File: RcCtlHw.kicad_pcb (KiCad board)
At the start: 2 copper layers, 26.7 x 41.9 mm, 30 parts, among them J1 USB_B_Mini, J2 Program, J3 TFT_LCD, SW1 On/Off, U1 TP4056, U2 ESP-M2, U3 ADS1015, U4 Joystick

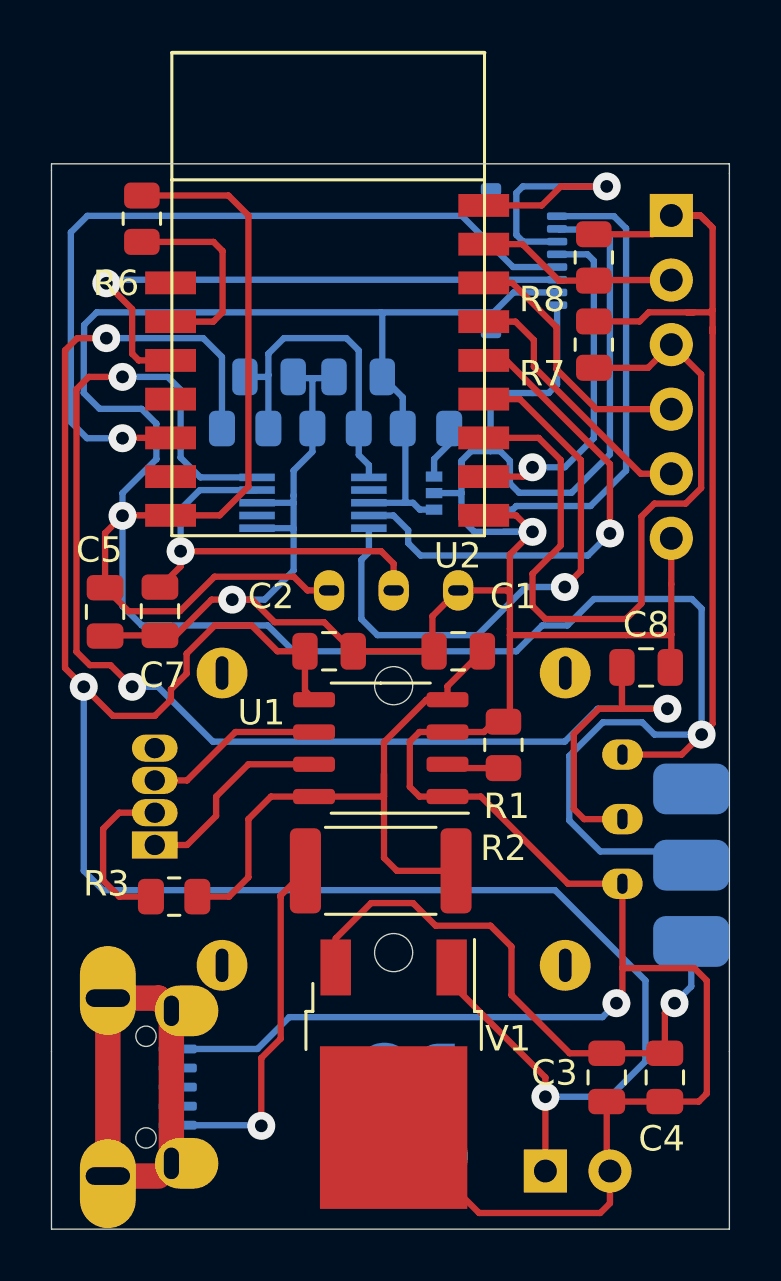
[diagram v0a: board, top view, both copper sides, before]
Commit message: Space things out
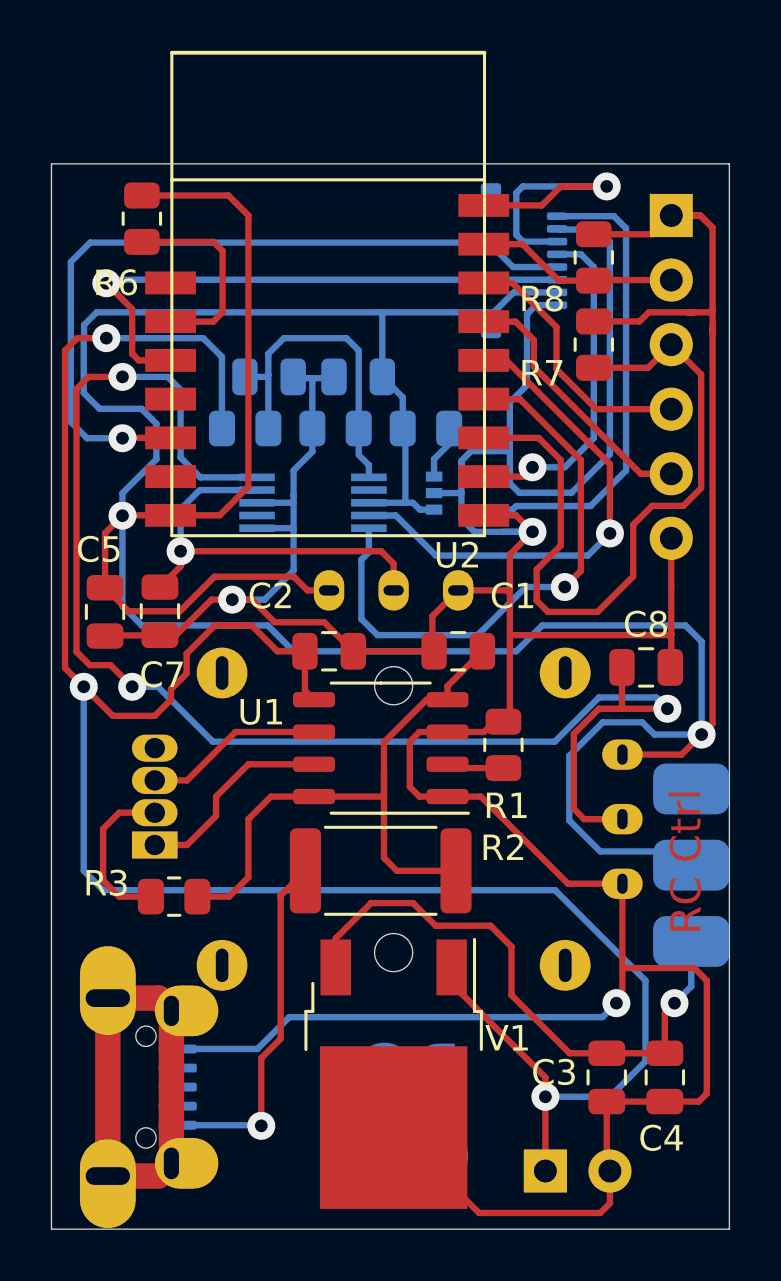
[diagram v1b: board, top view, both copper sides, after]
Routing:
- net +3V3: track 156.1 -> 154.5 mm
- net /TFT_SDA: track 31.9 -> 30.3 mm
- net /Flash: track 30.1 -> 28.7 mm
- net GND: track 155.2 -> 154.4 mm
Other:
- board text added: "RC Ctrl"
